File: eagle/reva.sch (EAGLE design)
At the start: 220 parts, among them IC1 LM555D, IC2 74HC174D, SW1 SWITCH-BRUH

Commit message: Save board state
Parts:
- removed DF16: RGB_LED_XL, flashing_ece_2025:RGB_LED_XL
- removed R76: (no value), adafruit:R-US_R0402
- removed SW1: SWITCH-BRUH, flashing_ece_2025:SWITCH-BRUH
- added C6: 100n, adafruit:C-USC0805
- added C7, C8, C9: 10u, adafruit:C-USC0805
- added H1, H2, H3, H4: MOUNT-HOLE3.3, holes:MOUNT-HOLE3.3
- added J1: TYPE-C-31-M-12, TYPE-C-31-M-12:TYPE-C-31-M-12
- added L1: LQH3NPN2R2MJRL, LQH3NPN2R2MJRL:LQH3NPN2R2MJRL
- added PWR: SWITCH-BRUH, flashing_ece_2025:SWITCH-BRUH
- added R108: 100, adafruit:R-US_R0402
- added R109: 75k, adafruit:R-US_R0402
- added SJ1: (no value), jumper:SJ
- added U1: TPS63002DRCR, TPS63001DRCR:TPS63001DRCR
- C2: value 100n -> 10u; device adafruit:C-USC0603 -> adafruit:C-USC0805
- C4: value 4u7 -> 10u
- R1, R2: value (none) -> 470
- R96, R97: value 100k -> 75k
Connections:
- net N$96 renamed TR
- net N$99 renamed CV
- removed net N$76: DF16.B+, DF16.G+, DF16.R+, R76.1
- removed net N$97: IC1.DIS, R96.1, R97.2
- new net 5VBUCK: C2.1, C8.1, C9.1, SJ1.1, U1.FB, U1.VOUT
- new net BUCK_IN: C7.1, PWR.C, R108.2, U1.VIN
- new net DIS: IC1.DIS, R109.2, R96.1, R97.2
- new net N$100: L1.1, U1.L1
- new net N$101: L1.2, U1.L2
- new net N$103: J1.VBUS, PWR.T1
- new net N$104: BT1.+, PWR.T2
- new net VINA: C6.1, R108.1, U1.EN, U1.PS/SYNC, U1.VINA
- net +5V: now also SJ1.2; no longer C2.1, R76.2
- net CLK_1HZ: now also IC2A.CLK
- net GND: now also BT1.-, C6.2, C7.2, C8.2, C9.2, J1.GND, U1.GND, U1.PGND, U1.POWER_PAD
- net N$98: now also R109.1
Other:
- note added: "CONTROL"
- note added: "PWR"

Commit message: Finish rough layout
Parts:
- C6: device adafruit:C-USC0805 -> adafruit:C-USC0603
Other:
- moved on the sheet: C1, IC2P

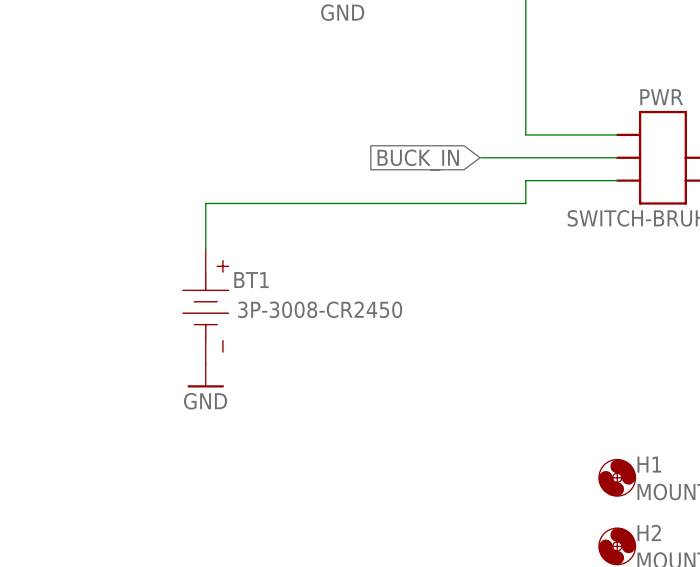
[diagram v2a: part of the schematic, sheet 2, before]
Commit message: Change battery holder, create BOM and PNP
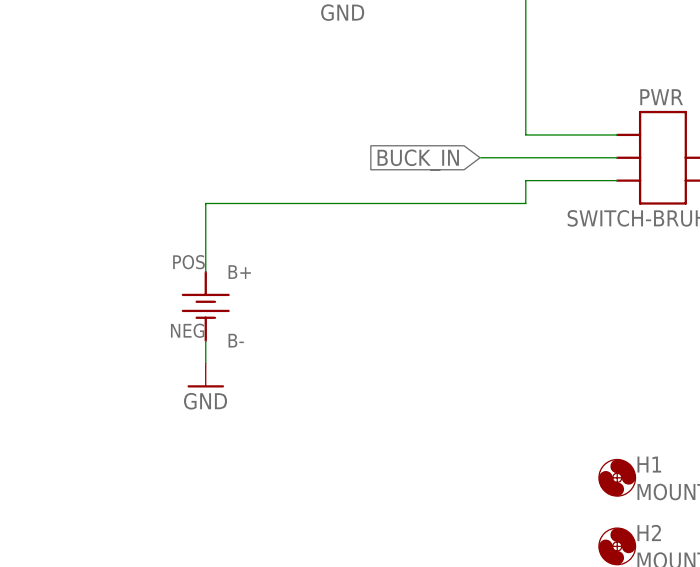
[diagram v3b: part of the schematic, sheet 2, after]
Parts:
- removed BT1: 3P-3008-CR2450, Battery_Holder:COIN-CELL-SMT-3P-3008-CR2450
- added BAT1: CR2450, flashing_ece_2025:CR2450
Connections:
- net GND: now also BAT1.B-; no longer BT1.-
- net N$104: now also BAT1.B+; no longer BT1.+

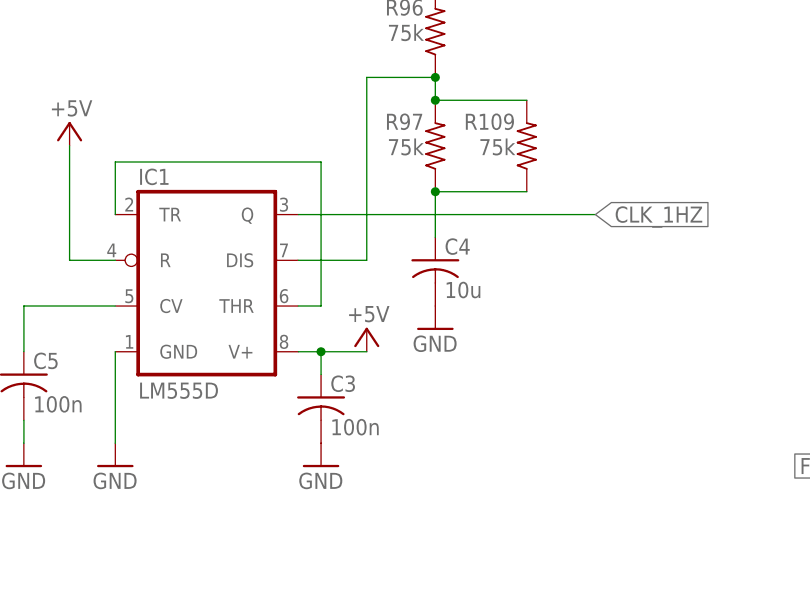
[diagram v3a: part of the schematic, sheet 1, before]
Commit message: Fix 555 error
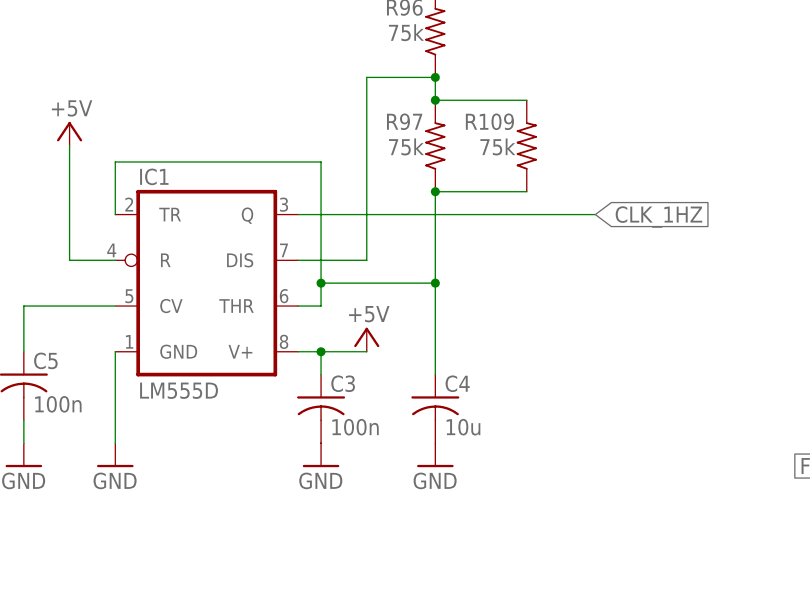
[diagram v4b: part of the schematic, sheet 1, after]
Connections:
- removed net N$98: C4.1, R109.1, R97.1
- net TR: now also C4.1, R109.1, R97.1
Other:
- moved on the sheet: C4
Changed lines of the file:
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@@
 <attribute name="VALUE" x="62.23" y="56.642" size="1.778" layer="96" rot="R180"/>
 </instance>
-<instance part="C4" gate="G$1" x="63.5" y="43.18" smashed="yes">
-<attribute name="NAME" x="64.516" y="43.815" size="1.778" layer="95"/>
-<attribute name="VALUE" x="64.516" y="38.989" size="1.778" layer="96"/>
+<instance part="C4" gate="G$1" x="63.5" y="27.94" smashed="yes">
+<attribute name="NAME" x="64.516" y="28.575" size="1.778" layer="95"/>
+<attribute name="VALUE" x="64.516" y="23.749" size="1.778" layer="96"/>
 </instance>
-<instance part="GND12" gate="1" x="63.5" y="35.56" smashed="yes">
-<attribute name="VALUE" x="60.96" y="33.02" size="1.778" layer="96"/>
+<instance part="GND12" gate="1" x="63.5" y="20.32" smashed="yes">
+<attribute name="VALUE" x="60.96" y="17.78" size="1.778" layer="96"/>
 </instance>
 <instance part="P+99" gate="1" x="63.5" y="76.2" smashed="yes">
@@
 <wire x1="27.94" y1="54.102" x2="50.8" y2="54.102" width="0.1524" layer="91"/>
 <pinref part="IC1" gate="A" pin="THR"/>
-<wire x1="50.8" y1="54.102" x2="50.8" y2="38.1" width="0.1524" layer="91"/>
+<wire x1="50.8" y1="54.102" x2="50.8" y2="40.64" width="0.1524" layer="91"/>
+<wire x1="50.8" y1="40.64" x2="50.8" y2="38.1" width="0.1524" layer="91"/>
 <wire x1="50.8" y1="38.1" x2="48.26" y2="38.1" width="0.1524" layer="91"/>
+<pinref part="C4" gate="G$1" pin="1"/>
+<pinref part="R97" gate="G$1" pin="1"/>
+<wire x1="63.5" y1="30.48" x2="63.5" y2="40.64" width="0.1524" layer="91"/>
+<pinref part="R109" gate="G$1" pin="1"/>
+<wire x1="63.5" y1="40.64" x2="63.5" y2="50.8" width="0.1524" layer="91"/>
+<wire x1="63.5" y1="50.8" x2="73.66" y2="50.8" width="0.1524" layer="91"/>
+<junction x="63.5" y="50.8"/>
+<wire x1="50.8" y1="40.64" x2="63.5" y2="40.64" width="0.1524" layer="91"/>
+<junction x="50.8" y="40.64"/>
+<junction x="63.5" y="40.64"/>
 </segment>
 </net>
@@
 </segment>
 </net>
-<net name="N$98" class="0">
-<segment>
-<pinref part="C4" gate="G$1" pin="1"/>
-<pinref part="R97" gate="G$1" pin="1"/>
-<wire x1="63.5" y1="45.72" x2="63.5" y2="50.8" width="0.1524" layer="91"/>
-<pinref part="R109" gate="G$1" pin="1"/>
-<wire x1="63.5" y1="50.8" x2="73.66" y2="50.8" width="0.1524" layer="91"/>
-<junction x="63.5" y="50.8"/>
-</segment>
-</net>

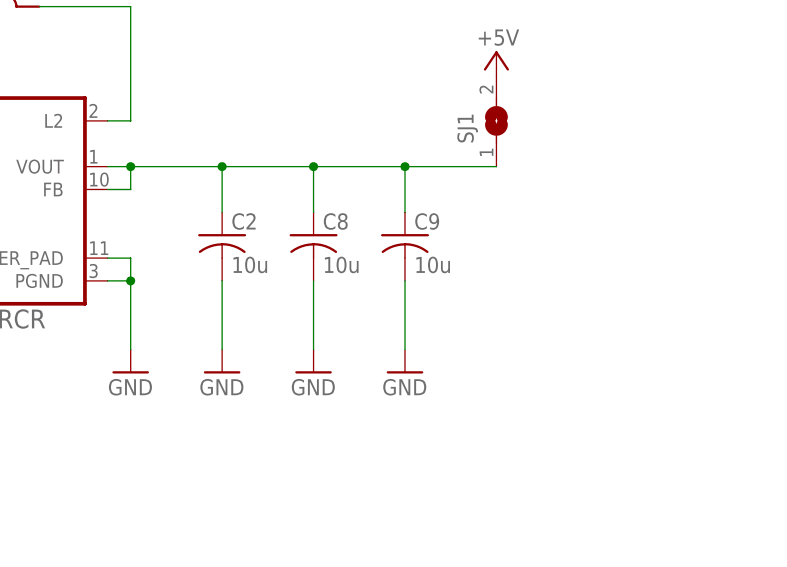
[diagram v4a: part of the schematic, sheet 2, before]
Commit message: Change buck to have 20uF Cout, increase inductor footprint size
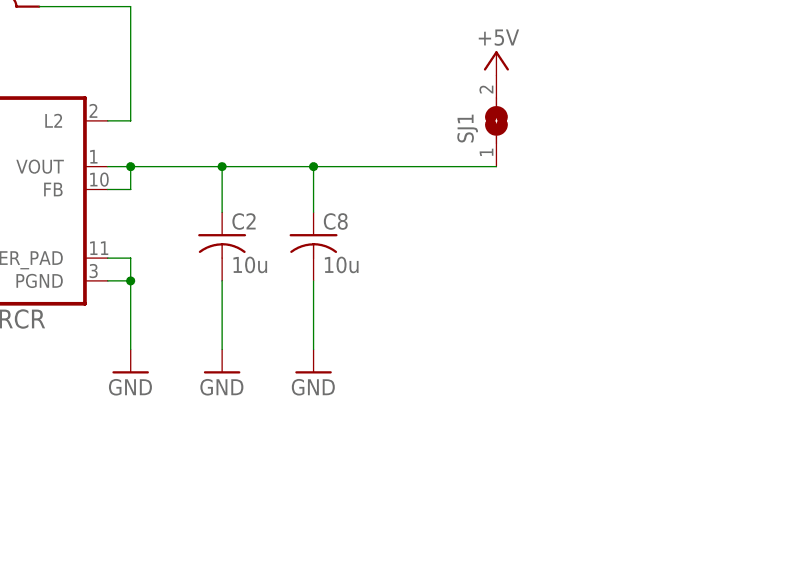
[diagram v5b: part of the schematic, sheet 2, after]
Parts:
- removed C9: 10u, adafruit:C-USC0805
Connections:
- net N$100 renamed L1
- net N$101 renamed L2
- net 5VBUCK: no longer C9.1
- net GND: no longer C9.2
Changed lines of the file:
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@@
 <part name="GND22" library="supply1" library_urn="urn:adsk.eagle:library:371" deviceset="GND" device=""/>
 <part name="GND23" library="supply1" library_urn="urn:adsk.eagle:library:371" deviceset="GND" device=""/>
-<part name="C9" library="adafruit" library_urn="urn:adsk.eagle:library:420" deviceset="C-US" device="C0805" package3d_urn="urn:adsk.eagle:package:6240337/1" value="10u"/>
-<part name="GND24" library="supply1" library_urn="urn:adsk.eagle:library:371" deviceset="GND" device=""/>
 <part name="SJ1" library="jumper" library_urn="urn:adsk.eagle:library:252" deviceset="SJ" device="" package3d_urn="urn:adsk.eagle:package:15471/1"/>
 <part name="P+102" library="supply1" library_urn="urn:adsk.eagle:library:371" deviceset="+5V" device=""/>
@@
 <attribute name="VALUE" x="271.78" y="111.76" size="1.778" layer="96"/>
 </instance>
-<instance part="C9" gate="G$1" x="284.48" y="129.54" smashed="yes">
-<attribute name="NAME" x="285.496" y="130.175" size="1.778" layer="95"/>
-<attribute name="VALUE" x="285.496" y="125.349" size="1.778" layer="96"/>
-</instance>
-<instance part="GND24" gate="1" x="284.48" y="114.3" smashed="yes">
-<attribute name="VALUE" x="281.94" y="111.76" size="1.778" layer="96"/>
-</instance>
 <instance part="SJ1" gate="1" x="294.64" y="142.24" smashed="yes" rot="R90">
 <attribute name="NAME" x="292.1" y="139.7" size="1.778" layer="95" rot="R90"/>
@@
 </segment>
 <segment>
-<pinref part="GND24" gate="1" pin="GND"/>
-<pinref part="C9" gate="G$1" pin="2"/>
-<wire x1="284.48" y1="116.84" x2="284.48" y2="124.46" width="0.1524" layer="91"/>
-</segment>
-<segment>
 <pinref part="GND10" gate="1" pin="GND"/>
 <pinref part="BAT1" gate="G$1" pin="B-"/>
@@
 </segment>
 </net>
-<net name="N$100" class="0">
+<net name="L1" class="0">
 <segment>
 <pinref part="U1" gate="A" pin="L1"/>
@@
 </segment>
 </net>
-<net name="N$101" class="0">
+<net name="L2" class="0">
 <segment>
 <pinref part="U1" gate="A" pin="L2"/>
@@
 <wire x1="254" y1="137.16" x2="264.16" y2="137.16" width="0.1524" layer="91"/>
 <junction x="254" y="137.16"/>
-<pinref part="C9" gate="G$1" pin="1"/>
 <wire x1="264.16" y1="137.16" x2="274.32" y2="137.16" width="0.1524" layer="91"/>
-<wire x1="274.32" y1="137.16" x2="284.48" y2="137.16" width="0.1524" layer="91"/>
-<wire x1="284.48" y1="132.08" x2="284.48" y2="137.16" width="0.1524" layer="91"/>
-<junction x="284.48" y="137.16"/>
 <pinref part="C8" gate="G$1" pin="1"/>
 <wire x1="274.32" y1="132.08" x2="274.32" y2="137.16" width="0.1524" layer="91"/>
@@
 <wire x1="264.16" y1="132.08" x2="264.16" y2="137.16" width="0.1524" layer="91"/>
 <junction x="264.16" y="137.16"/>
-<wire x1="284.48" y1="137.16" x2="294.64" y2="137.16" width="0.1524" layer="91"/>
+<wire x1="274.32" y1="137.16" x2="294.64" y2="137.16" width="0.1524" layer="91"/>
 <pinref part="SJ1" gate="1" pin="1"/>
 </segment>

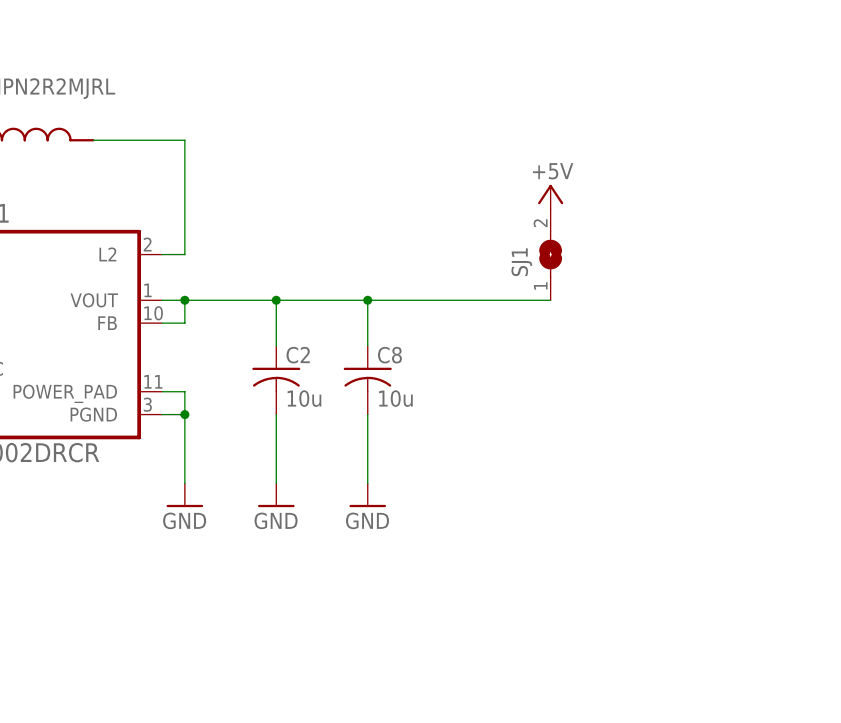
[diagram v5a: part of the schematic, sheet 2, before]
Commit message: Add resistive feedback to TP63000
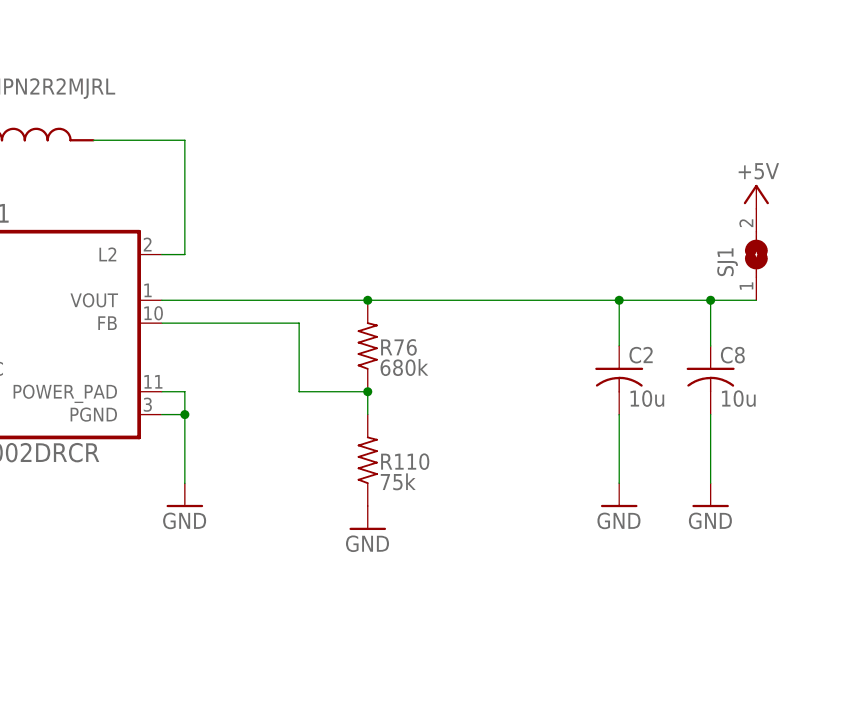
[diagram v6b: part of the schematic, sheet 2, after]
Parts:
- added R110: 75k, adafruit:R-US_R0402
- added R76: 680k, adafruit:R-US_R0402
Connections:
- new net N$76: R110.2, R76.1, U1.FB
- net 5VBUCK: now also R76.2; no longer U1.FB
- net GND: now also R110.1
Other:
- moved on the sheet: C2, C8, SJ1
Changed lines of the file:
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@@
 <part name="H4" library="holes" library_urn="urn:adsk.eagle:library:237" deviceset="MOUNT-HOLE" device="3.3" package3d_urn="urn:adsk.eagle:package:14278/1"/>
 <part name="BAT1" library="flashing_ece_2025" deviceset="CR2450" device=""/>
+<part name="R76" library="adafruit" deviceset="R-US_" device="R0402" value="680k"/>
+<part name="R110" library="adafruit" deviceset="R-US_" device="R0402" value="75k"/>
+<part name="GND24" library="supply1" library_urn="urn:adsk.eagle:library:371" deviceset="GND" device=""/>
 </parts>
 <sheets>
@@
 <attribute name="VALUE" x="185.42" y="111.76" size="1.778" layer="96"/>
 </instance>
-<instance part="C2" gate="G$1" x="264.16" y="129.54" smashed="yes">
-<attribute name="NAME" x="265.176" y="130.175" size="1.778" layer="95"/>
-<attribute name="VALUE" x="265.176" y="125.349" size="1.778" layer="96"/>
-</instance>
-<instance part="C8" gate="G$1" x="274.32" y="129.54" smashed="yes">
-<attribute name="NAME" x="275.336" y="130.175" size="1.778" layer="95"/>
-<attribute name="VALUE" x="275.336" y="125.349" size="1.778" layer="96"/>
-</instance>
-<instance part="GND22" gate="1" x="264.16" y="114.3" smashed="yes">
-<attribute name="VALUE" x="261.62" y="111.76" size="1.778" layer="96"/>
-</instance>
-<instance part="GND23" gate="1" x="274.32" y="114.3" smashed="yes">
-<attribute name="VALUE" x="271.78" y="111.76" size="1.778" layer="96"/>
-</instance>
-<instance part="SJ1" gate="1" x="294.64" y="142.24" smashed="yes" rot="R90">
-<attribute name="NAME" x="292.1" y="139.7" size="1.778" layer="95" rot="R90"/>
-<attribute name="VALUE" x="298.45" y="139.7" size="1.778" layer="96" rot="R90"/>
+<instance part="C2" gate="G$1" x="302.26" y="129.54" smashed="yes">
+<attribute name="NAME" x="303.276" y="130.175" size="1.778" layer="95"/>
+<attribute name="VALUE" x="303.276" y="125.349" size="1.778" layer="96"/>
+</instance>
+<instance part="C8" gate="G$1" x="312.42" y="129.54" smashed="yes">
+<attribute name="NAME" x="313.436" y="130.175" size="1.778" layer="95"/>
+<attribute name="VALUE" x="313.436" y="125.349" size="1.778" layer="96"/>
+</instance>
+<instance part="GND22" gate="1" x="302.26" y="114.3" smashed="yes">
+<attribute name="VALUE" x="299.72" y="111.76" size="1.778" layer="96"/>
+</instance>
+<instance part="GND23" gate="1" x="312.42" y="114.3" smashed="yes">
+<attribute name="VALUE" x="309.88" y="111.76" size="1.778" layer="96"/>
+</instance>
+<instance part="SJ1" gate="1" x="317.5" y="142.24" smashed="yes" rot="R90">
+<attribute name="NAME" x="314.96" y="139.7" size="1.778" layer="95" rot="R90"/>
+<attribute name="VALUE" x="321.31" y="139.7" size="1.778" layer="96" rot="R90"/>
 </instance>
-<instance part="P+102" gate="1" x="294.64" y="149.86" smashed="yes">
-<attribute name="VALUE" x="297.18" y="152.4" size="1.778" layer="96" rot="R180"/>
+<instance part="P+102" gate="1" x="317.5" y="149.86" smashed="yes">
+<attribute name="VALUE" x="320.04" y="152.4" size="1.778" layer="96" rot="R180"/>
 </instance>
 <instance part="H1" gate="G$1" x="114.3" y="83.82" smashed="yes">
@@
 </instance>
 <instance part="BAT1" gate="G$1" x="68.58" y="104.14" smashed="yes"/>
+<instance part="R76" gate="G$1" x="274.32" y="132.08" smashed="yes" rot="R90">
+<attribute name="NAME" x="275.59" y="131.0386" size="1.778" layer="95"/>
+<attribute name="VALUE" x="275.59" y="128.778" size="1.778" layer="96"/>
+</instance>
+<instance part="R110" gate="G$1" x="274.32" y="119.38" smashed="yes" rot="R90">
+<attribute name="NAME" x="275.59" y="118.3386" size="1.778" layer="95"/>
+<attribute name="VALUE" x="275.59" y="116.078" size="1.778" layer="96"/>
+</instance>
+<instance part="GND24" gate="1" x="274.32" y="111.76" smashed="yes">
+<attribute name="VALUE" x="271.78" y="109.22" size="1.778" layer="96"/>
+</instance>
 </instances>
 <busses>
@@
 <pinref part="GND22" gate="1" pin="GND"/>
 <pinref part="C2" gate="G$1" pin="2"/>
-<wire x1="264.16" y1="116.84" x2="264.16" y2="124.46" width="0.1524" layer="91"/>
+<wire x1="302.26" y1="116.84" x2="302.26" y2="124.46" width="0.1524" layer="91"/>
 </segment>
 <segment>
 <pinref part="GND23" gate="1" pin="GND"/>
 <pinref part="C8" gate="G$1" pin="2"/>
-<wire x1="274.32" y1="116.84" x2="274.32" y2="124.46" width="0.1524" layer="91"/>
+<wire x1="312.42" y1="116.84" x2="312.42" y2="124.46" width="0.1524" layer="91"/>
 </segment>
 <segment>
@@
 <wire x1="68.58" y1="96.52" x2="68.58" y2="99.06" width="0.1524" layer="91"/>
 </segment>
+<segment>
+<pinref part="R110" gate="G$1" pin="1"/>
+<pinref part="GND24" gate="1" pin="GND"/>
+</segment>
 </net>
 <net name="L1" class="0">
@@
 <net name="5VBUCK" class="0">
 <segment>
-<pinref part="U1" gate="A" pin="FB"/>
-<wire x1="251.46" y1="134.62" x2="254" y2="134.62" width="0.1524" layer="91"/>
-<wire x1="254" y1="134.62" x2="254" y2="137.16" width="0.1524" layer="91"/>
 <pinref part="U1" gate="A" pin="VOUT"/>
-<wire x1="254" y1="137.16" x2="251.46" y2="137.16" width="0.1524" layer="91"/>
-<wire x1="254" y1="137.16" x2="264.16" y2="137.16" width="0.1524" layer="91"/>
-<junction x="254" y="137.16"/>
-<wire x1="264.16" y1="137.16" x2="274.32" y2="137.16" width="0.1524" layer="91"/>
+<wire x1="251.46" y1="137.16" x2="274.32" y2="137.16" width="0.1524" layer="91"/>
+<wire x1="274.32" y1="137.16" x2="302.26" y2="137.16" width="0.1524" layer="91"/>
+<wire x1="302.26" y1="137.16" x2="312.42" y2="137.16" width="0.1524" layer="91"/>
 <pinref part="C8" gate="G$1" pin="1"/>
-<wire x1="274.32" y1="132.08" x2="274.32" y2="137.16" width="0.1524" layer="91"/>
-<junction x="274.32" y="137.16"/>
+<wire x1="312.42" y1="132.08" x2="312.42" y2="137.16" width="0.1524" layer="91"/>
+<junction x="312.42" y="137.16"/>
 <pinref part="C2" gate="G$1" pin="1"/>
-<wire x1="264.16" y1="132.08" x2="264.16" y2="137.16" width="0.1524" layer="91"/>
-<junction x="264.16" y="137.16"/>
-<wire x1="274.32" y1="137.16" x2="294.64" y2="137.16" width="0.1524" layer="91"/>
+<wire x1="302.26" y1="132.08" x2="302.26" y2="137.16" width="0.1524" layer="91"/>
+<junction x="302.26" y="137.16"/>
+<wire x1="312.42" y1="137.16" x2="317.5" y2="137.16" width="0.1524" layer="91"/>
 <pinref part="SJ1" gate="1" pin="1"/>
+<pinref part="R76" gate="G$1" pin="2"/>
+<junction x="274.32" y="137.16"/>
 </segment>
 </net>
@@
 </segment>
 </net>
+<net name="N$76" class="0">
+<segment>
+<pinref part="R110" gate="G$1" pin="2"/>
+<pinref part="R76" gate="G$1" pin="1"/>
+<wire x1="274.32" y1="124.46" x2="274.32" y2="127" width="0.1524" layer="91"/>
+<wire x1="274.32" y1="127" x2="266.7" y2="127" width="0.1524" layer="91"/>
+<wire x1="266.7" y1="127" x2="266.7" y2="134.62" width="0.1524" layer="91"/>
+<junction x="274.32" y="127"/>
+<pinref part="U1" gate="A" pin="FB"/>
+<wire x1="266.7" y1="134.62" x2="251.46" y2="134.62" width="0.1524" layer="91"/>
+</segment>
+</net>
